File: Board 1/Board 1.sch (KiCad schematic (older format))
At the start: 77 parts, among them J10 NEG. NULL, J18 POS. NULL, J2 Y INPUT, J4 ???, J5 OUTPUT, J6 +15V, J7 GND, J8 -15V, J9 GAIN TRIM, T1 TIP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

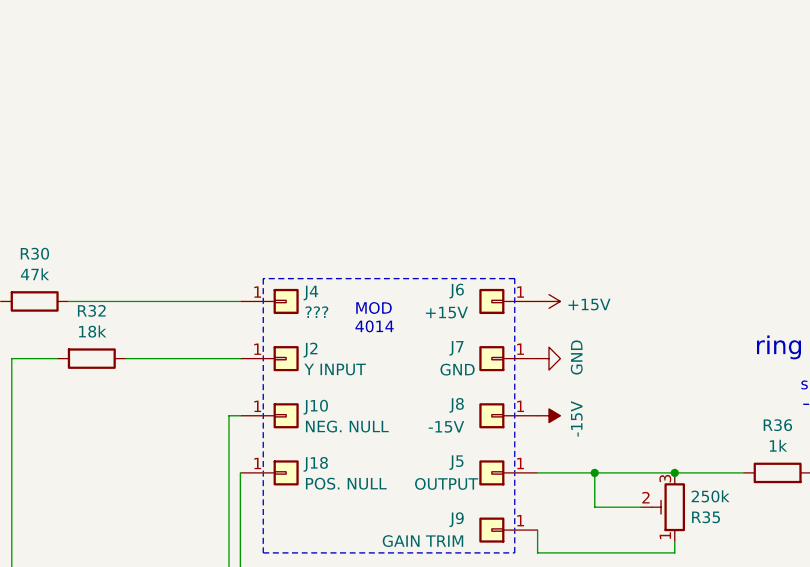
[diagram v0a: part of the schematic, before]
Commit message: fix J3 vs J4 typo
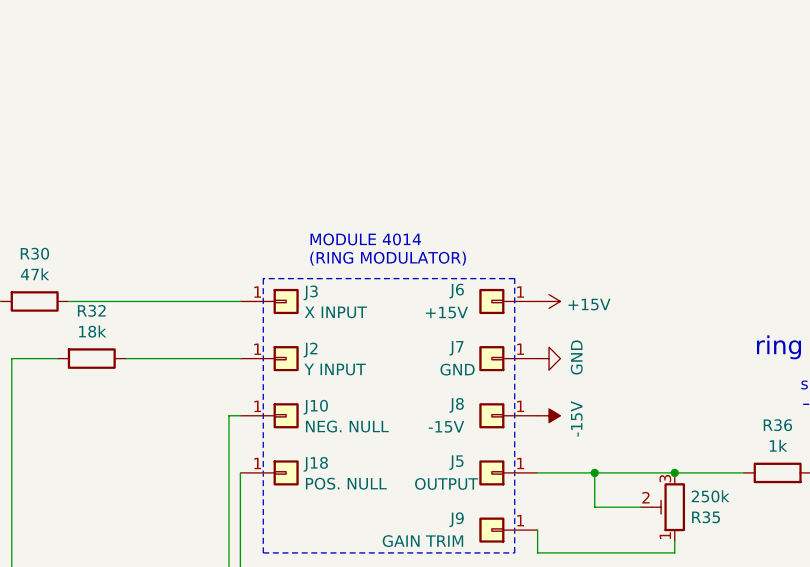
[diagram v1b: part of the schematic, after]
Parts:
- J3: renamed from J4; value ??? -> X INPUT
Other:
- note added: "MODULE 4014\n(RING MODULATOR)"
- note removed: "MOD\n4014"
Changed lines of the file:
@@
 	8900 5650 8700 5650
 $Comp
-L Connector_Generic:Conn_01x01 J4
+L Connector_Generic:Conn_01x01 J3
 U 1 1 60C8763D
 P 8400 7950
-F 0 "J4" H 8480 7992 50  0000 L CNN
-F 1 "???" H 8480 7901 50  0000 L CNN
+F 0 "J3" H 8480 7992 50  0000 L CNN
+F 1 "X INPUT" H 8480 7901 50  0000 L CNN
 F 2 "" H 8400 7950 50  0001 C CNN
 F 3 "~" H 8400 7950 50  0001 C CNN
@@
 	-1   0    0    1
 $EndComp
-Text Notes 8700 8100 0    50   ~ 0
-MOD\n4014
+Text Notes 8500 7800 0    50   ~ 0
+MODULE 4014\n(RING MODULATOR)
 Wire Notes Line
 	8300 7850 8300 9050

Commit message: some fixes
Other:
- note added: "which is the SLEEVE of T1 (upper left)"
- note added: "which is the T4 pin\nof the mic preamp out\nsee middle right"
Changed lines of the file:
@@
 Wire Notes Line
 	2600 1600 2550 1600
-Wire Notes Line
-	1850 1400 2600 1400
 Text Notes 1800 1350 0    50   ~ 0
 sleeve: pre amp output
@@
 Text Notes 8950 5850 0    50   ~ 0
 should also connect TIP to 'env. follower input'
+Text Notes 8950 6000 0    50   ~ 0
+which is the SLEEVE of T1 (upper left)
+Text Notes 1150 1700 0    50   ~ 0
+which is the T4 pin\nof the mic preamp out\nsee middle right
+Wire Notes Line
+	1100 4100 11400 4100
+Wire Notes Line
+	11400 4100 11400 5900
+Wire Notes Line
+	11400 5900 9450 5900
+Wire Notes Line
+	1100 1400 2600 1400
+Wire Notes Line
+	1100 1400 1100 4100
 $EndSCHEMATC

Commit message: fixes
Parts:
- added R18: 1k, symbol Device:R
- A1, A2, A3, A4: Notes (none) -> If TL071, remove caps between pin 1 and 8
- C1, C24: value 0.1uF -> 100nF; Notes (none) -> ceramic
- C10: value 1.0uF -> 2nF; Notes (none) -> ceramic
- C12, C15, C16, C3, C6: Notes (none) -> ceramic
- C13, C14, C18, C19, C20, C21: value 10uF -> 10uF 35V; Notes (none) -> electrolytic
- C22, C23: value 1uF -> 1uF 35V; Notes (none) -> electrolytic
- C7: value 1.0uF -> 1uF 35V; Notes (none) -> electrolytic
- C8: value 1.0uF -> 100nF; Notes (none) -> ceramic
- C9: value 1.0uF -> 10nF; Notes (none) -> ceramic
- R13: value 2.7k -> 27k
- R14: value 2.7k -> 270k
- R15: value 2.7k -> 1M
- R16: value 1.6M -> 1.5M
- R23: value 100k AUD -> 100k LOG
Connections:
- net at A3.6, R17.1: now also R18.2; no longer T2.1 (Pin_1)
- new net: R18.1, T2.1 (Pin_1)
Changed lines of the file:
@@
 P 15100 1300
 F 0 "C22" H 15215 1346 50  0000 L CNN
-F 1 "1uF" H 15215 1255 50  0000 L CNN
+F 1 "1uF 35V" H 15215 1255 50  0000 L CNN
 F 2 "" H 15138 1150 50  0001 C CNN
 F 3 "~" H 15100 1300 50  0001 C CNN
+F 4 "electrolytic" H 15100 1300 50  0001 C CNN "Notes"
 	1    15100 1300
 	1    0    0    -1
@@
 P 15100 1800
 F 0 "C23" H 15215 1846 50  0000 L CNN
-F 1 "1uF" H 15215 1755 50  0000 L CNN
+F 1 "1uF 35V" H 15215 1755 50  0000 L CNN
 F 2 "" H 15138 1650 50  0001 C CNN
 F 3 "~" H 15100 1800 50  0001 C CNN
+F 4 "electrolytic" H 15100 1800 50  0001 C CNN "Notes"
 	1    15100 1800
 	1    0    0    -1
@@
 F 2 "" H 3850 2550 50  0001 C CNN
 F 3 "http://www.ti.com/lit/ds/symlink/lm101a-n.pdf" H 3850 2650 50  0001 C CNN
+F 4 "If TL071, remove caps between pin 1 and 8" H 3800 2500 50  0001 C CNN "Notes"
 	1    3800 2500
 	1    0    0    -1
@@
 F 2 "" H 5800 3300 50  0001 C CNN
 F 3 "http://www.ti.com/lit/ds/symlink/lm101a-n.pdf" H 5800 3400 50  0001 C CNN
+F 4 "If TL071, remove caps between pin 1 and 8" H 5750 3250 50  0001 C CNN "Notes"
 	1    5750 3250
 	1    0    0    -1
@@
 F 2 "" H 9300 2350 50  0001 C CNN
 F 3 "http://www.ti.com/lit/ds/symlink/lm101a-n.pdf" H 9300 2450 50  0001 C CNN
+F 4 "If TL071, remove caps between pin 1 and 8" H 9250 2300 50  0001 C CNN "Notes"
 	1    9250 2300
 	1    0    0    -1
@@
 F 2 "" H 4088 2000 50  0001 C CNN
 F 3 "~" H 4050 2150 50  0001 C CNN
+F 4 "ceramic" H 4050 2150 50  0001 C CNN "Notes"
 	1    4050 2150
 	0    1    1    0
@@
 P 2500 2300
 F 0 "C1" H 2615 2346 50  0000 L CNN
-F 1 "0.1uF" H 2615 2255 50  0000 L CNN
+F 1 "100nF" H 2615 2255 50  0000 L CNN
 F 2 "" H 2538 2150 50  0001 C CNN
 F 3 "~" H 2500 2300 50  0001 C CNN
+F 4 "ceramic" H 2500 2300 50  0001 C CNN "Notes"
 	1    2500 2300
 	1    0    0    -1
@@
 F 2 "" H 6088 2700 50  0001 C CNN
 F 3 "~" H 6050 2850 50  0001 C CNN
+F 4 "ceramic" H 6050 2850 50  0001 C CNN "Notes"
 	1    6050 2850
 	0    1    1    0
@@
 F 2 "" H 9488 1800 50  0001 C CNN
 F 3 "~" H 9450 1950 50  0001 C CNN
+F 4 "ceramic" H 9450 1950 50  0001 C CNN "Notes"
 	1    9450 1950
 	0    1    1    0
@@
 P 6900 3400
 F 0 "C7" H 7015 3446 50  0000 L CNN
-F 1 "1.0uF" H 7015 3355 50  0000 L CNN
+F 1 "1uF 35V" H 7015 3355 50  0000 L CNN
 F 2 "" H 6938 3250 50  0001 C CNN
 F 3 "~" H 6900 3400 50  0001 C CNN
+F 4 "electrolytic" H 6900 3400 50  0001 C CNN "Notes"
 	1    6900 3400
 	1    0    0    -1
@@
 P 7150 3250
 F 0 "R13" V 6943 3250 50  0000 C CNN
-F 1 "2.7k" V 7034 3250 50  0000 C CNN
+F 1 "27k" V 7034 3250 50  0000 C CNN
 F 2 "" V 7080 3250 50  0001 C CNN
 F 3 "~" H 7150 3250 50  0001 C CNN
@@
 P 7350 3400
 F 0 "C8" H 7465 3446 50  0000 L CNN
-F 1 "1.0uF" H 7465 3355 50  0000 L CNN
+F 1 "100nF" H 7465 3355 50  0000 L CNN
 F 2 "" H 7388 3250 50  0001 C CNN
 F 3 "~" H 7350 3400 50  0001 C CNN
+F 4 "ceramic" H 7350 3400 50  0001 C CNN "Notes"
 	1    7350 3400
 	1    0    0    -1
@@
 P 7600 3250
 F 0 "R14" V 7393 3250 50  0000 C CNN
-F 1 "2.7k" V 7484 3250 50  0000 C CNN
+F 1 "270k" V 7484 3250 50  0000 C CNN
 F 2 "" V 7530 3250 50  0001 C CNN
 F 3 "~" H 7600 3250 50  0001 C CNN
@@
 P 7800 3400
 F 0 "C9" H 7915 3446 50  0000 L CNN
-F 1 "1.0uF" H 7915 3355 50  0000 L CNN
+F 1 "10nF" H 7915 3355 50  0000 L CNN
 F 2 "" H 7838 3250 50  0001 C CNN
 F 3 "~" H 7800 3400 50  0001 C CNN
+F 4 "ceramic" H 7800 3400 50  0001 C CNN "Notes"
 	1    7800 3400
 	1    0    0    -1
@@
 P 8050 3250
 F 0 "R15" V 7843 3250 50  0000 C CNN
-F 1 "2.7k" V 7934 3250 50  0000 C CNN
+F 1 "1M" V 7934 3250 50  0000 C CNN
 F 2 "" V 7980 3250 50  0001 C CNN
 F 3 "~" H 8050 3250 50  0001 C CNN
@@
 P 8250 3400
 F 0 "C10" H 8365 3446 50  0000 L CNN
-F 1 "1.0uF" H 8365 3355 50  0000 L CNN
+F 1 "2nF" H 8365 3355 50  0000 L CNN
 F 2 "" H 8288 3250 50  0001 C CNN
 F 3 "~" H 8250 3400 50  0001 C CNN
+F 4 "ceramic" H 8250 3400 50  0001 C CNN "Notes"
 	1    8250 3400
 	1    0    0    -1
@@
 P 7650 1500
 F 0 "R16" V 7443 1500 50  0000 C CNN
-F 1 "1.6M" V 7534 1500 50  0000 C CNN
+F 1 "1.5M" V 7534 1500 50  0000 C CNN
 F 2 "" V 7580 1500 50  0001 C CNN
 F 3 "~" H 7650 1500 50  0001 C CNN
@@
 Wire Wire Line
 	9950 1500 9950 2300
-Connection ~ 9950 2300
-Wire Wire Line
-	9950 2300 10700 2300
 $Comp
 L Connector_Generic:Conn_01x01 T3
@@
 P 3550 5550
 F 0 "R23" H 3481 5596 50  0000 R CNN
-F 1 "100k AUD" H 3481 5505 50  0000 R CNN
+F 1 "100k LOG" H 3481 5505 50  0000 R CNN
 F 2 "" H 3550 5550 50  0001 C CNN
 F 3 "~" H 3550 5550 50  0001 C CNN
@@
 P 3850 5550
 F 0 "C24" V 3598 5550 50  0000 C CNN
-F 1 "0.1uF" V 3689 5550 50  0000 C CNN
+F 1 "100nF" V 3689 5550 50  0000 C CNN
 F 2 "" H 3888 5400 50  0001 C CNN
 F 3 "~" H 3850 5550 50  0001 C CNN
+F 4 "ceramic" H 3850 5550 50  0001 C CNN "Notes"
 	1    3850 5550
 	0    1    1    0
@@
 F 2 "" H 5638 5150 50  0001 C CNN
 F 3 "~" H 5600 5300 50  0001 C CNN
+F 4 "ceramic" H 5600 5300 50  0001 C CNN "Notes"
 	1    5600 5300
 	0    1    1    0
@@
 F 2 "" H 5450 5700 50  0001 C CNN
 F 3 "http://www.ti.com/lit/ds/symlink/lm101a-n.pdf" H 5450 5800 50  0001 C CNN
+F 4 "If TL071, remove caps between pin 1 and 8" H 5400 5650 50  0001 C CNN "Notes"
 	1    5400 5650
 	1    0    0    -1
@@
 F 2 "" H 6088 4550 50  0001 C CNN
 F 3 "~" H 6050 4700 50  0001 C CNN
+F 4 "ceramic" H 6050 4700 50  0001 C CNN "Notes"
 	1    6050 4700
 	0    1    1    0
@@
 P 6100 7950
 F 0 "C18" V 6355 7950 50  0000 C CNN
-F 1 "10uF" V 6264 7950 50  0000 C CNN
+F 1 "10uF 35V" V 6264 7950 50  0000 C CNN
 F 2 "" H 6138 7800 50  0001 C CNN
 F 3 "~" H 6100 7950 50  0001 C CNN
+F 4 "electrolytic" H 6100 7950 50  0001 C CNN "Notes"
 	1    6100 7950
 	0    -1   -1   0
@@
 P 6400 7950
 F 0 "C19" V 6145 7950 50  0000 C CNN
-F 1 "10uF" V 6236 7950 50  0000 C CNN
+F 1 "10uF 35V" V 6236 7950 50  0000 C CNN
 F 2 "" H 6438 7800 50  0001 C CNN
 F 3 "~" H 6400 7950 50  0001 C CNN
+F 4 "electrolytic" H 6400 7950 50  0001 C CNN "Notes"
 	1    6400 7950
 	0    1    1    0
@@
 P 4200 4850
 F 0 "C13" V 4455 4850 50  0000 C CNN
-F 1 "10uF" V 4364 4850 50  0000 C CNN
+F 1 "10uF 35V" V 4364 4850 50  0000 C CNN
 F 2 "" H 4238 4700 50  0001 C CNN
 F 3 "~" H 4200 4850 50  0001 C CNN
+F 4 "electrolytic" H 4200 4850 50  0001 C CNN "Notes"
 	1    4200 4850
 	0    -1   -1   0
@@
 P 4500 4850
 F 0 "C14" V 4245 4850 50  0000 C CNN
-F 1 "10uF" V 4336 4850 50  0000 C CNN
+F 1 "10uF 35V" V 4336 4850 50  0000 C CNN
 F 2 "" H 4538 4700 50  0001 C CNN
 F 3 "~" H 4500 4850 50  0001 C CNN
+F 4 "electrolytic" H 4500 4850 50  0001 C CNN "Notes"
 	1    4500 4850
 	0    1    1    0
@@
 P 6100 9200
 F 0 "C20" V 6355 9200 50  0000 C CNN
-F 1 "10uF" V 6264 9200 50  0000 C CNN
+F 1 "10uF 35V" V 6264 9200 50  0000 C CNN
 F 2 "" H 6138 9050 50  0001 C CNN
 F 3 "~" H 6100 9200 50  0001 C CNN
+F 4 "electrolytic" H 6100 9200 50  0001 C CNN "Notes"
 	1    6100 9200
 	0    -1   -1   0
@@
 P 6400 9200
 F 0 "C21" V 6145 9200 50  0000 C CNN
-F 1 "10uF" V 6236 9200 50  0000 C CNN
+F 1 "10uF 35V" V 6236 9200 50  0000 C CNN
 F 2 "" H 6438 9050 50  0001 C CNN
 F 3 "~" H 6400 9200 50  0001 C CNN
+F 4 "electrolytic" H 6400 9200 50  0001 C CNN "Notes"
 	1    6400 9200
 	0    1    1    0
@@
 Wire Notes Line
 	1100 1400 1100 4100
+$Comp
+L Device:R R18
+U 1 1 60F37C69
+P 10300 2300
+F 0 "R18" V 10093 2300 50  0000 C CNN
+F 1 "1k" V 10184 2300 50  0000 C CNN
+F 2 "" V 10230 2300 50  0001 C CNN
+F 3 "~" H 10300 2300 50  0001 C CNN
+	1    10300 2300
+	0    1    1    0
+$EndComp
+Wire Wire Line
+	10450 2300 10700 2300
+Wire Wire Line
+	10150 2300 9950 2300
+Connection ~ 9950 2300
 $EndSCHEMATC

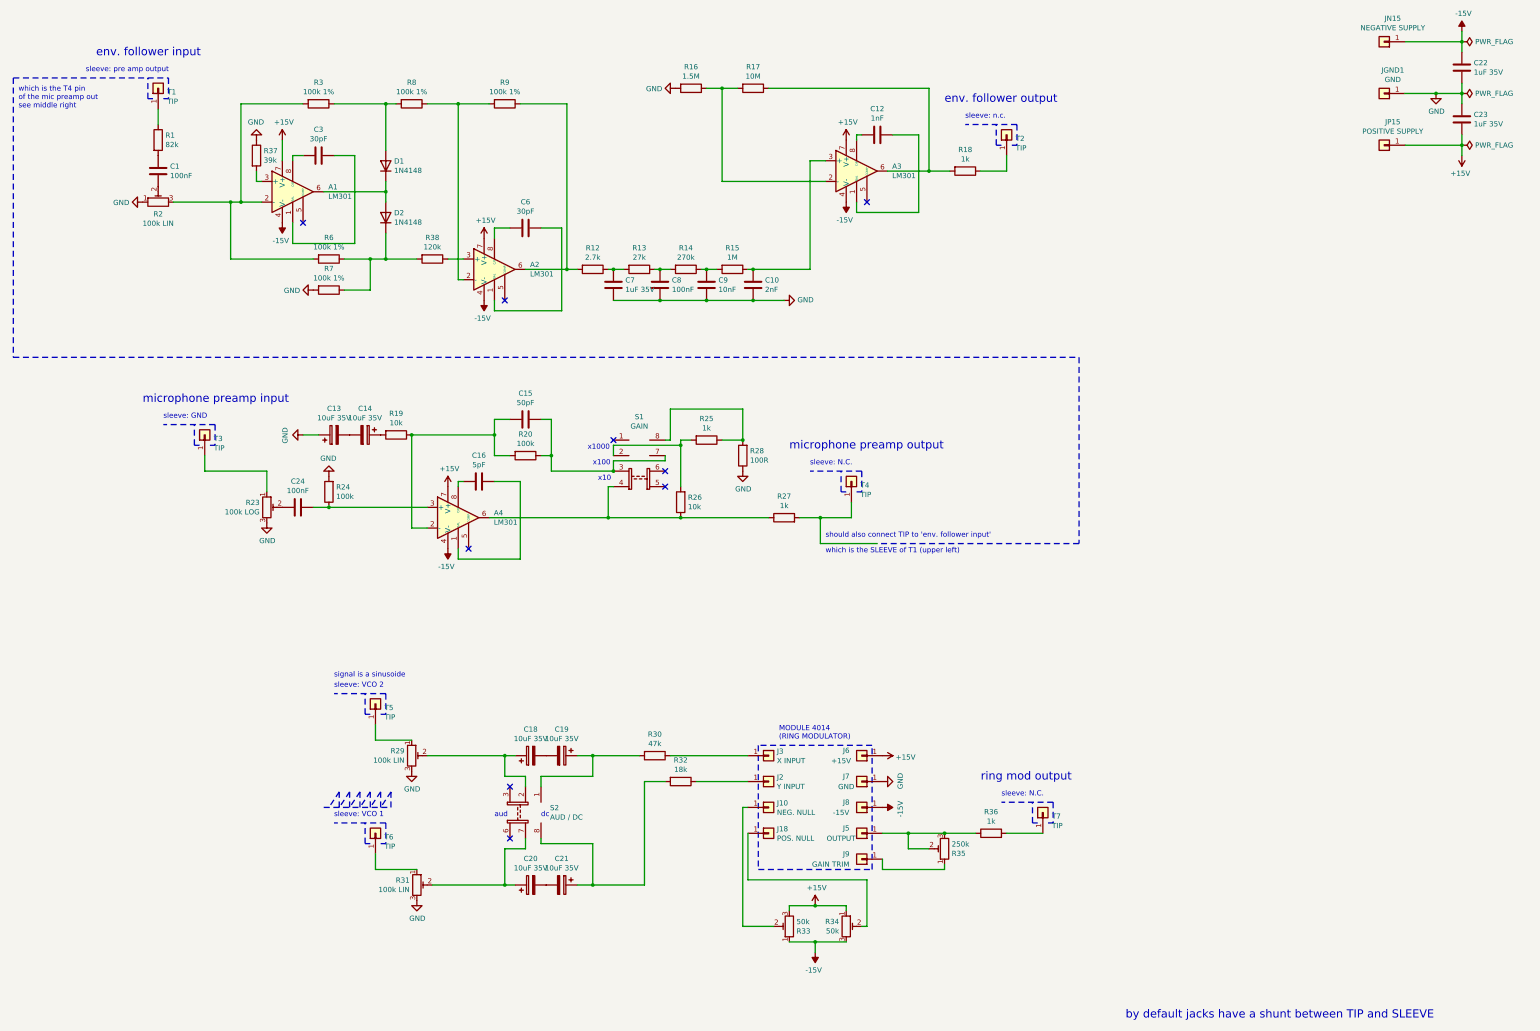
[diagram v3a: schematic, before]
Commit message: add submodule; add jacks placeholders
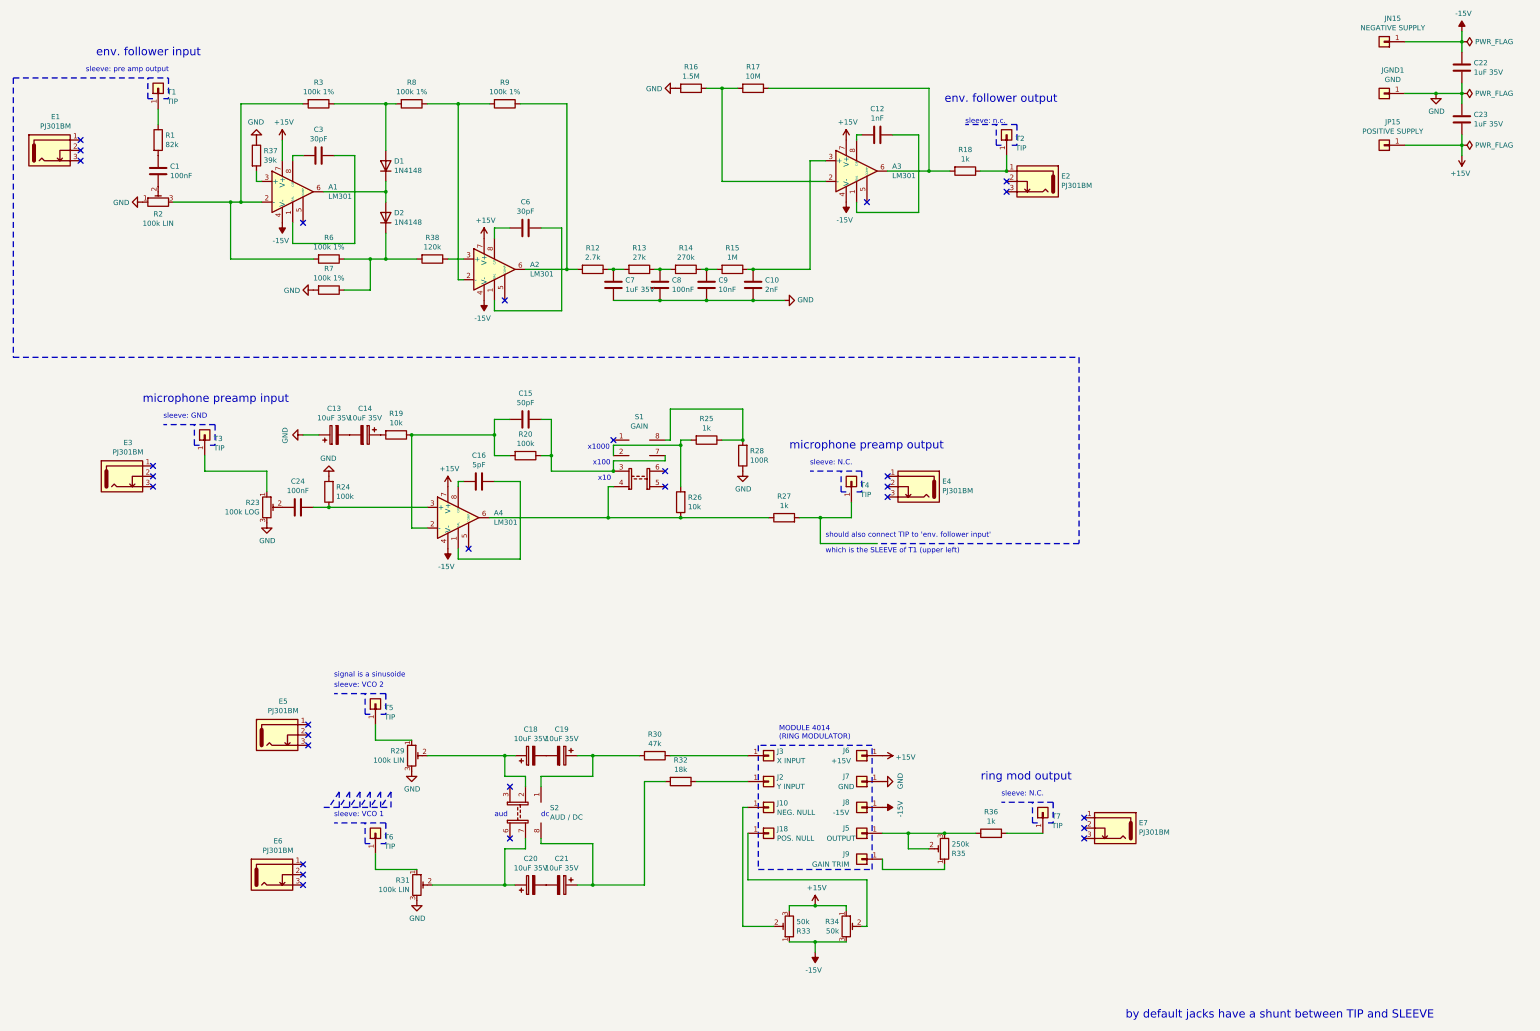
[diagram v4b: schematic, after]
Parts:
- added E1, E2, E3, E4, E5, E6, E7: PJ301BM, symbol w_connector:PJ301BM
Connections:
- net at R18.1, T2.1 (Pin_1): now also E2.1
- no-connect marks 9 -> 29
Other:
- note removed: "which is the T4 pin\nof the mic preamp out\nsee middle right"
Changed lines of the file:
@@
 Wire Notes Line
 	10800 2050 10750 2050
-Text Notes 10300 1800 0    50   ~ 0
+Text Notes 10300 1850 0    50   ~ 0
 sleeve: n.c.
 Text Notes 10100 1650 0    79   ~ 0
@@
 Text Notes 8950 6000 0    50   ~ 0
 which is the SLEEVE of T1 (upper left)
-Text Notes 1150 1700 0    50   ~ 0
-which is the T4 pin\nof the mic preamp out\nsee middle right
 Wire Notes Line
 	1100 4100 11400 4100
@@
 Wire Notes Line
 	11400 5900 9450 5900
-Wire Notes Line
-	1100 1400 2600 1400
-Wire Notes Line
-	1100 1400 1100 4100
 $Comp
 L Device:R R18
@@
 	10150 2300 9950 2300
 Connection ~ 9950 2300
+$Comp
+L w_connector:PJ301BM E2
+U 1 1 600FEB3E
+P 10800 2400
+F 0 "E2" H 10372 2451 50  0000 R CNN
+F 1 "PJ301BM" H 10372 2360 50  0000 R CNN
+F 2 "" H 10950 2500 50  0001 C CNN
+F 3 "https://www.thonk.co.uk/shop/3-5mm-jacks/" H 10950 2500 50  0001 C CNN
+	1    10800 2400
+	-1   0    0    -1
+$EndComp
+$Comp
+L w_connector:PJ301BM E4
+U 1 1 601006C8
+P 9650 5350
+F 0 "E4" H 9222 5401 50  0000 R CNN
+F 1 "PJ301BM" H 9222 5310 50  0000 R CNN
+F 2 "" H 9800 5450 50  0001 C CNN
+F 3 "https://www.thonk.co.uk/shop/3-5mm-jacks/" H 9800 5450 50  0001 C CNN
+	1    9650 5350
+	-1   0    0    -1
+$EndComp
+$Comp
+L w_connector:PJ301BM E3
+U 1 1 6010151E
+P 2350 5250
+F 0 "E3" H 2208 5575 50  0000 C CNN
+F 1 "PJ301BM" H 2208 5484 50  0000 C CNN
+F 2 "" H 2500 5350 50  0001 C CNN
+F 3 "https://www.thonk.co.uk/shop/3-5mm-jacks/" H 2500 5350 50  0001 C CNN
+	1    2350 5250
+	1    0    0    -1
+$EndComp
+$Comp
+L w_connector:PJ301BM E5
+U 1 1 6010250C
+P 3850 7750
+F 0 "E5" H 3708 8075 50  0000 C CNN
+F 1 "PJ301BM" H 3708 7984 50  0000 C CNN
+F 2 "" H 4000 7850 50  0001 C CNN
+F 3 "https://www.thonk.co.uk/shop/3-5mm-jacks/" H 4000 7850 50  0001 C CNN
+	1    3850 7750
+	1    0    0    -1
+$EndComp
+$Comp
+L w_connector:PJ301BM E6
+U 1 1 60103205
+P 3800 9100
+F 0 "E6" H 3658 9425 50  0000 C CNN
+F 1 "PJ301BM" H 3658 9334 50  0000 C CNN
+F 2 "" H 3950 9200 50  0001 C CNN
+F 3 "https://www.thonk.co.uk/shop/3-5mm-jacks/" H 3950 9200 50  0001 C CNN
+	1    3800 9100
+	1    0    0    -1
+$EndComp
+$Comp
+L w_connector:PJ301BM E7
+U 1 1 601037C2
+P 11550 8650
+F 0 "E7" H 11122 8701 50  0000 R CNN
+F 1 "PJ301BM" H 11122 8610 50  0000 R CNN
+F 2 "" H 11700 8750 50  0001 C CNN
+F 3 "https://www.thonk.co.uk/shop/3-5mm-jacks/" H 11700 8750 50  0001 C CNN
+	1    11550 8650
+	-1   0    0    -1
+$EndComp
+Connection ~ 10700 2300
+NoConn ~ 10700 2400
+NoConn ~ 10700 2500
+$Comp
+L w_connector:PJ301BM E1
+U 1 1 600FE280
+P 1650 2100
+F 0 "E1" H 1508 2425 50  0000 C CNN
+F 1 "PJ301BM" H 1508 2334 50  0000 C CNN
+F 2 "" H 1800 2200 50  0001 C CNN
+F 3 "https://www.thonk.co.uk/shop/3-5mm-jacks/" H 1800 2200 50  0001 C CNN
+	1    1650 2100
+	1    0    0    -1
+$EndComp
+Wire Notes Line
+	1100 1400 1100 4100
+Wire Notes Line
+	1100 1400 2600 1400
+NoConn ~ 1750 2000
+NoConn ~ 1750 2100
+NoConn ~ 1750 2200
+NoConn ~ 9550 5250
+NoConn ~ 9550 5350
+NoConn ~ 9550 5450
+NoConn ~ 2450 5150
+NoConn ~ 2450 5250
+NoConn ~ 2450 5350
+NoConn ~ 3900 9000
+NoConn ~ 3900 9100
+NoConn ~ 3900 9200
+NoConn ~ 3950 7650
+NoConn ~ 3950 7750
+NoConn ~ 3950 7850
+NoConn ~ 11450 8550
+NoConn ~ 11450 8650
+NoConn ~ 11450 8750
 $EndSCHEMATC
